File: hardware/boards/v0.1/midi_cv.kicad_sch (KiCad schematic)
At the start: 20 parts, among them J10 MIDI_OUT/THRU, J11 MIDI_IN, U19 TLP2362TPR_E, U35 TS5A23159RSE

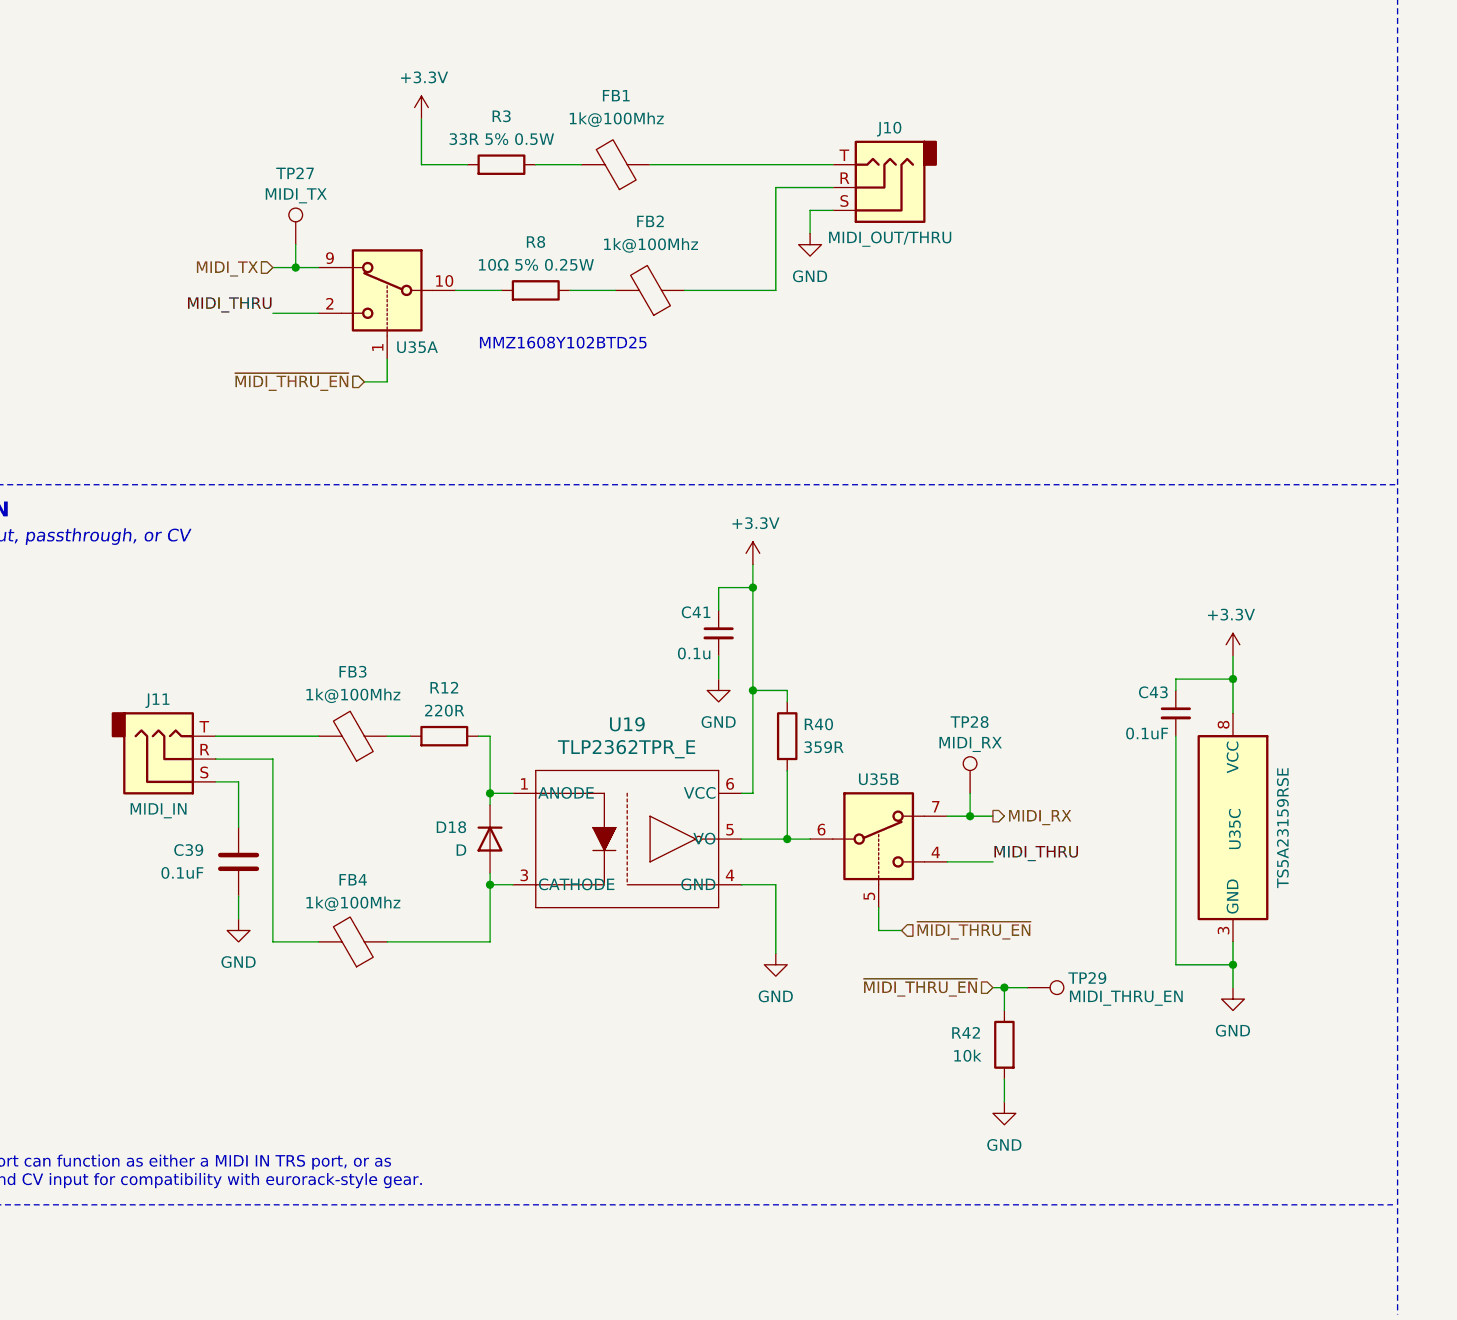
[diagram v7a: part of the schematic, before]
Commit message: feat: remove analog MIDI thru
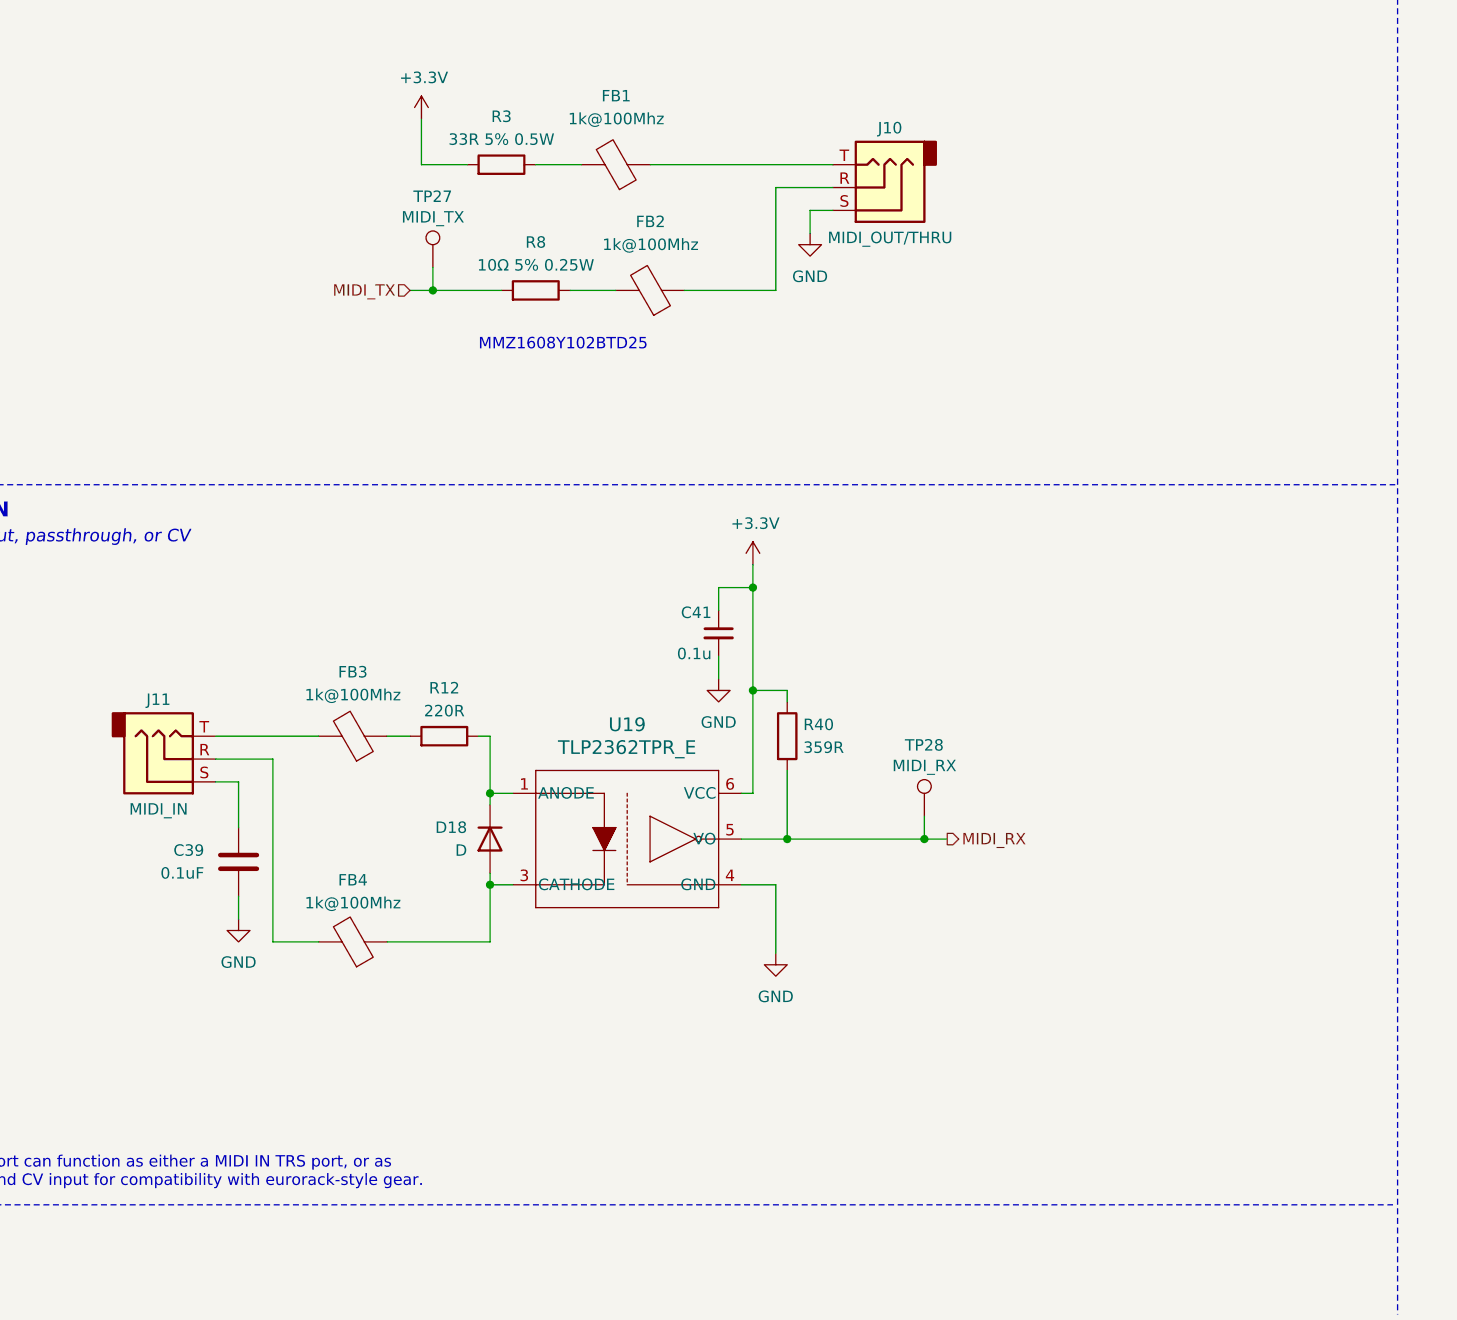
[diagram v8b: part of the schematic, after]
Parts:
- removed C43: 0.1uF, Capacitor_SMD:C_0603_1608Metric, symbol Device:C_Small
- removed R42: 10k, Resistor_SMD:R_0603_1608Metric, symbol Device:R
- removed TP29: MIDI_THRU_EN, TestPoint:TestPoint_Pad_D1.0mm, symbol Connector:TestPoint
- removed U35: TS5A23159RSE, Package_DFN_QFN:Texas_R-PUQFN-N10, symbol Analog_Switch:TS5A23159RSE
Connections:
- net MIDI_RX: now also R40.2, U19.5 (VO)
- net MIDI_TX: now also R8.2
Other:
- moved on the sheet: TP27, TP28
